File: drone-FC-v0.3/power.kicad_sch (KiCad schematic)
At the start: 5 parts, among them U1 MCP1727-3302xSN

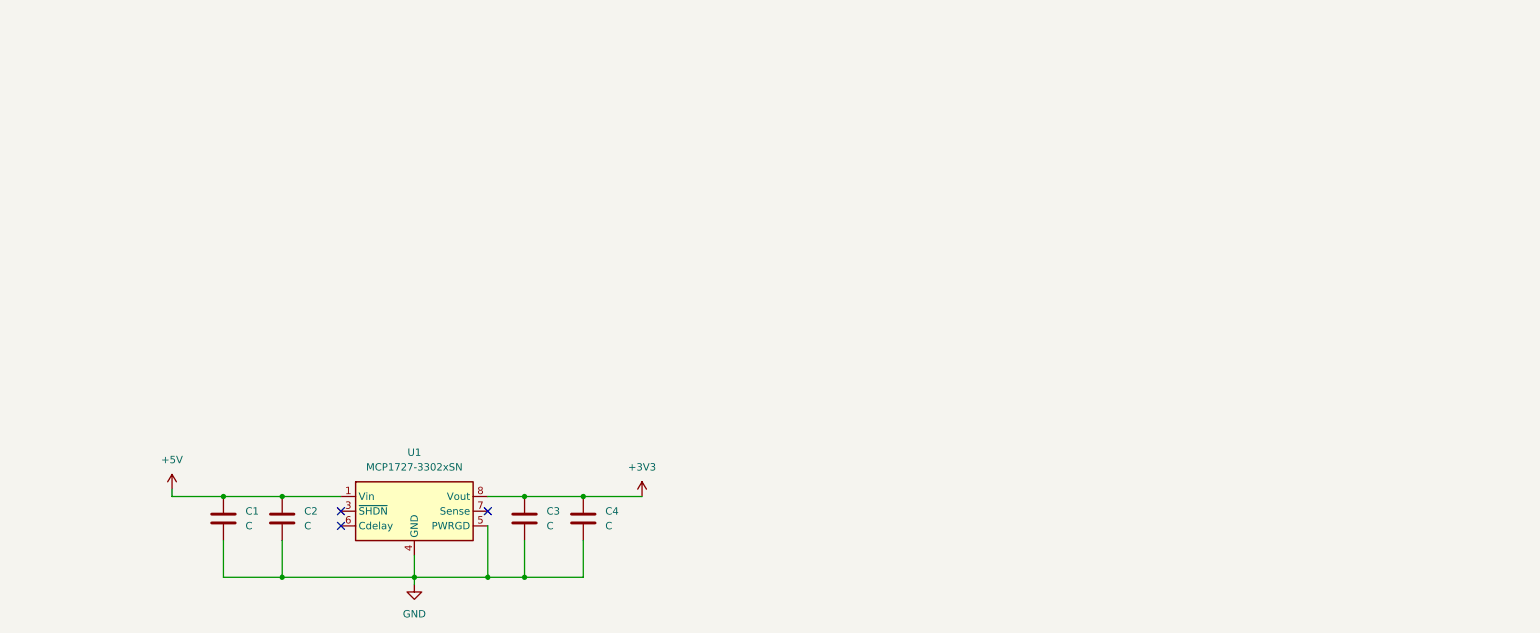
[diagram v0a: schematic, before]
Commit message: what
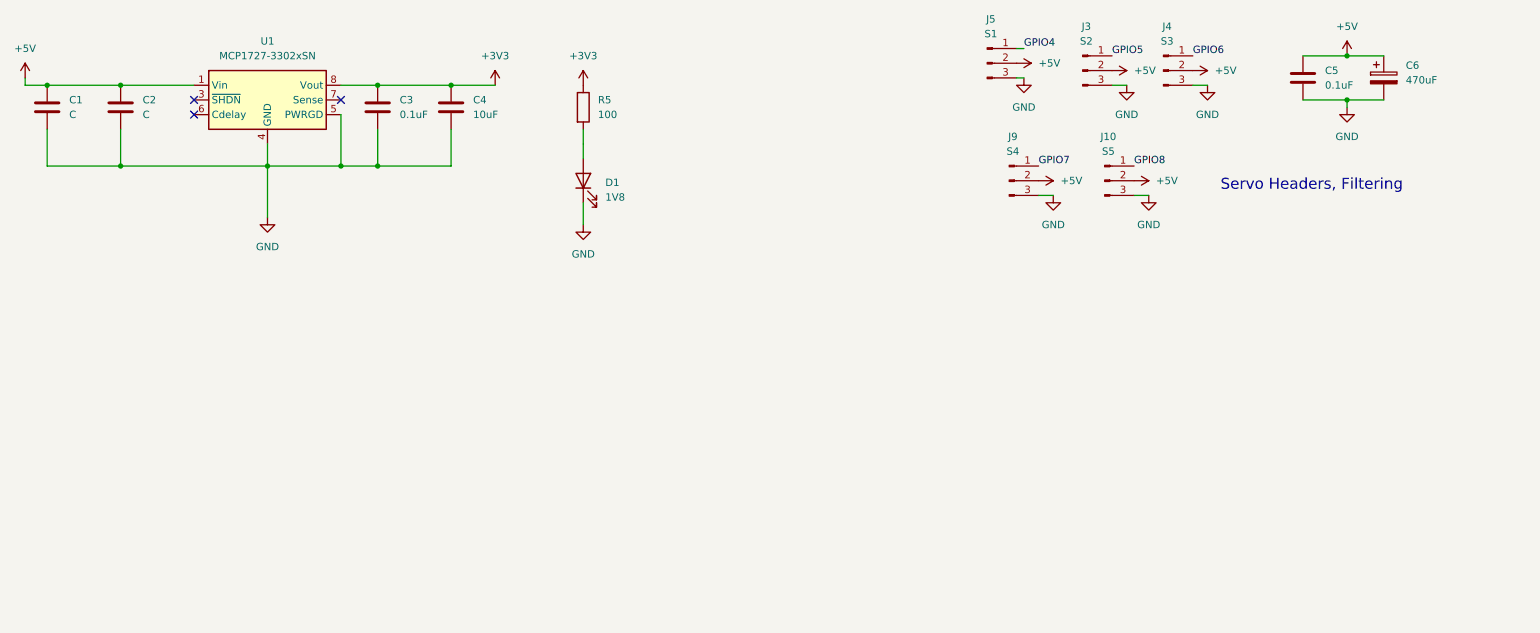
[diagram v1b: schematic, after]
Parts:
- added C5: 0.1uF, Capacitor_SMD:C_0603_1608Metric, symbol Device:C
- added C6: 470uF, Capacitor_THT:CP_Radial_D10.0mm_P5.00mm, symbol Device:C_Polarized
- added D1: 1V8, LED_SMD:LED_0603_1608Metric, symbol Device:LED
- added J10: S5, Connector_PinHeader_2.54mm:PinHeader_1x03_P2.54mm_Vertical, symbol Connector:Conn_01x03_Pin
- added J3: S2, Connector_PinHeader_2.54mm:PinHeader_1x03_P2.54mm_Vertical, symbol Connector:Conn_01x03_Pin
- added J4: S3, Connector_PinHeader_2.54mm:PinHeader_1x03_P2.54mm_Vertical, symbol Connector:Conn_01x03_Pin
- added J5: S1, Connector_PinHeader_2.54mm:PinHeader_1x03_P2.54mm_Vertical, symbol Connector:Conn_01x03_Pin
- added J9: S4, Connector_PinHeader_2.54mm:PinHeader_1x03_P2.54mm_Vertical, symbol Connector:Conn_01x03_Pin
- added R5: 100, Resistor_SMD:R_0603_1608Metric, symbol Device:R
- C3: value C -> 0.1uF
- C4: value C -> 10uF; LCSC (none) -> C1691
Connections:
- net +3V3: now also R5.1
- net +5V: now also C5.1, C6.1, J10.2 (Pin_2), J3.2 (Pin_2), J4.2 (Pin_2), J5.2 (Pin_2), J9.2 (Pin_2)
- net GND: now also C5.2, C6.2, D1.1 (K), J10.3 (Pin_3), J3.3 (Pin_3), J4.3 (Pin_3), J5.3 (Pin_3), J9.3 (Pin_3)
- new net: D1.2 (A), R5.2
- new net GPIO4: J5.1 (Pin_1)
- new net GPIO5: J3.1 (Pin_1)
- new net GPIO6: J4.1 (Pin_1)
- new net GPIO7: J9.1 (Pin_1)
- new net GPIO8: J10.1 (Pin_1)
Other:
- note added: "Servo Headers, Filtering"
- moved on the sheet: C1, C2, C3, C4, U1

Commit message: whatever
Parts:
- removed C6: 470uF, Capacitor_THT:CP_Radial_D10.0mm_P5.00mm, symbol Device:C_Polarized
- added C6: something idk yet, Capacitor_THT:C_Radial_D6.3mm_H5.0mm_P2.50mm, symbol Device:C
- J10: value S5 -> M1
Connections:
- net +5V: now also C6.1
- net GND: now also C6.2

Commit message: "global labels added"
"global labels added"
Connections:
- net GPIO4 renamed GPIO 4
- net GPIO5 renamed GPIO 5
- net GPIO6 renamed GPIO 6
- net GPIO7 renamed GPIO 7
- net GPIO8 renamed GPIO 8
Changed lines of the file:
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@@
 		)
 	)
-	(label "GPIO5"
+	(global_label "GPIO 5"
+		(shape input)
 		(at 223.52 24.13 0)
+		(fields_autoplaced yes)
 		(effects
 			(font
 				(size 1.27 1.27)
 			)
-			(justify left bottom)
+			(justify left)
+		)
+		(property "Intersheetrefs" "${INTERSHEET_REFS}"
+			(at 233.1576 24.13 0)
+			(hide yes)
+			(show_name no)
+			(do_not_autoplace no)
+			(effects
+				(font
+					(size 1.27 1.27)
+				)
+				(justify left)
+			)
 		)
 	)
-	(label "GPIO6"
-		(at 237.49 24.13 0)
+	(global_label "GPIO 4"
+		(shape input)
+		(at 208.28 22.86 0)
+		(fields_autoplaced yes)
 		(effects
 			(font
 				(size 1.27 1.27)
 			)
-			(justify left bottom)
+			(justify left)
+		)
+		(property "Intersheetrefs" "${INTERSHEET_REFS}"
+			(at 217.9176 22.86 0)
+			(hide yes)
+			(show_name no)
+			(do_not_autoplace no)
+			(effects
+				(font
+					(size 1.27 1.27)
+				)
+				(justify left)
+			)
 		)
 	)
-	(label "GPIO7"
+	(global_label "GPIO 7"
+		(shape input)
 		(at 210.82 43.18 0)
+		(fields_autoplaced yes)
 		(effects
 			(font
 				(size 1.27 1.27)
 			)
-			(justify left bottom)
+			(justify left)
+		)
+		(property "Intersheetrefs" "${INTERSHEET_REFS}"
+			(at 220.4576 43.18 0)
+			(hide yes)
+			(show_name no)
+			(do_not_autoplace no)
+			(effects
+				(font
+					(size 1.27 1.27)
+				)
+				(justify left)
+			)
 		)
 	)
-	(label "GPIO8"
-		(at 227.33 43.18 0)
+	(global_label "GPIO 6"
+		(shape input)
+		(at 237.49 24.13 0)
+		(fields_autoplaced yes)
 		(effects
 			(font
 				(size 1.27 1.27)
 			)
-			(justify left bottom)
+			(justify left)
+		)
+		(property "Intersheetrefs" "${INTERSHEET_REFS}"
+			(at 247.1276 24.13 0)
+			(hide yes)
+			(show_name no)
+			(do_not_autoplace no)
+			(effects
+				(font
+					(size 1.27 1.27)
+				)
+				(justify left)
+			)
 		)
 	)
-	(label "GPIO4"
-		(at 208.28 22.86 0)
+	(global_label "GPIO 8"
+		(shape input)
+		(at 227.33 43.18 0)
+		(fields_autoplaced yes)
 		(effects
 			(font
 				(size 1.27 1.27)
 			)
-			(justify left bottom)
+			(justify left)
+		)
+		(property "Intersheetrefs" "${INTERSHEET_REFS}"
+			(at 236.9676 43.18 0)
+			(hide yes)
+			(show_name no)
+			(do_not_autoplace no)
+			(effects
+				(font
+					(size 1.27 1.27)
+				)
+				(justify left)
+			)
 		)
 	)
